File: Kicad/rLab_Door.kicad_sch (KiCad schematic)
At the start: 15 parts, among them J1 ACT_1, J10 I2C DISPLAY, J2 V_IN, J3 ACT_2, J4 BATTERY, J5 NPX_1, J6 NPX_2, J7 TAMPER, J8 WIEGAND KEYPAD, J9 NFC SERIAL

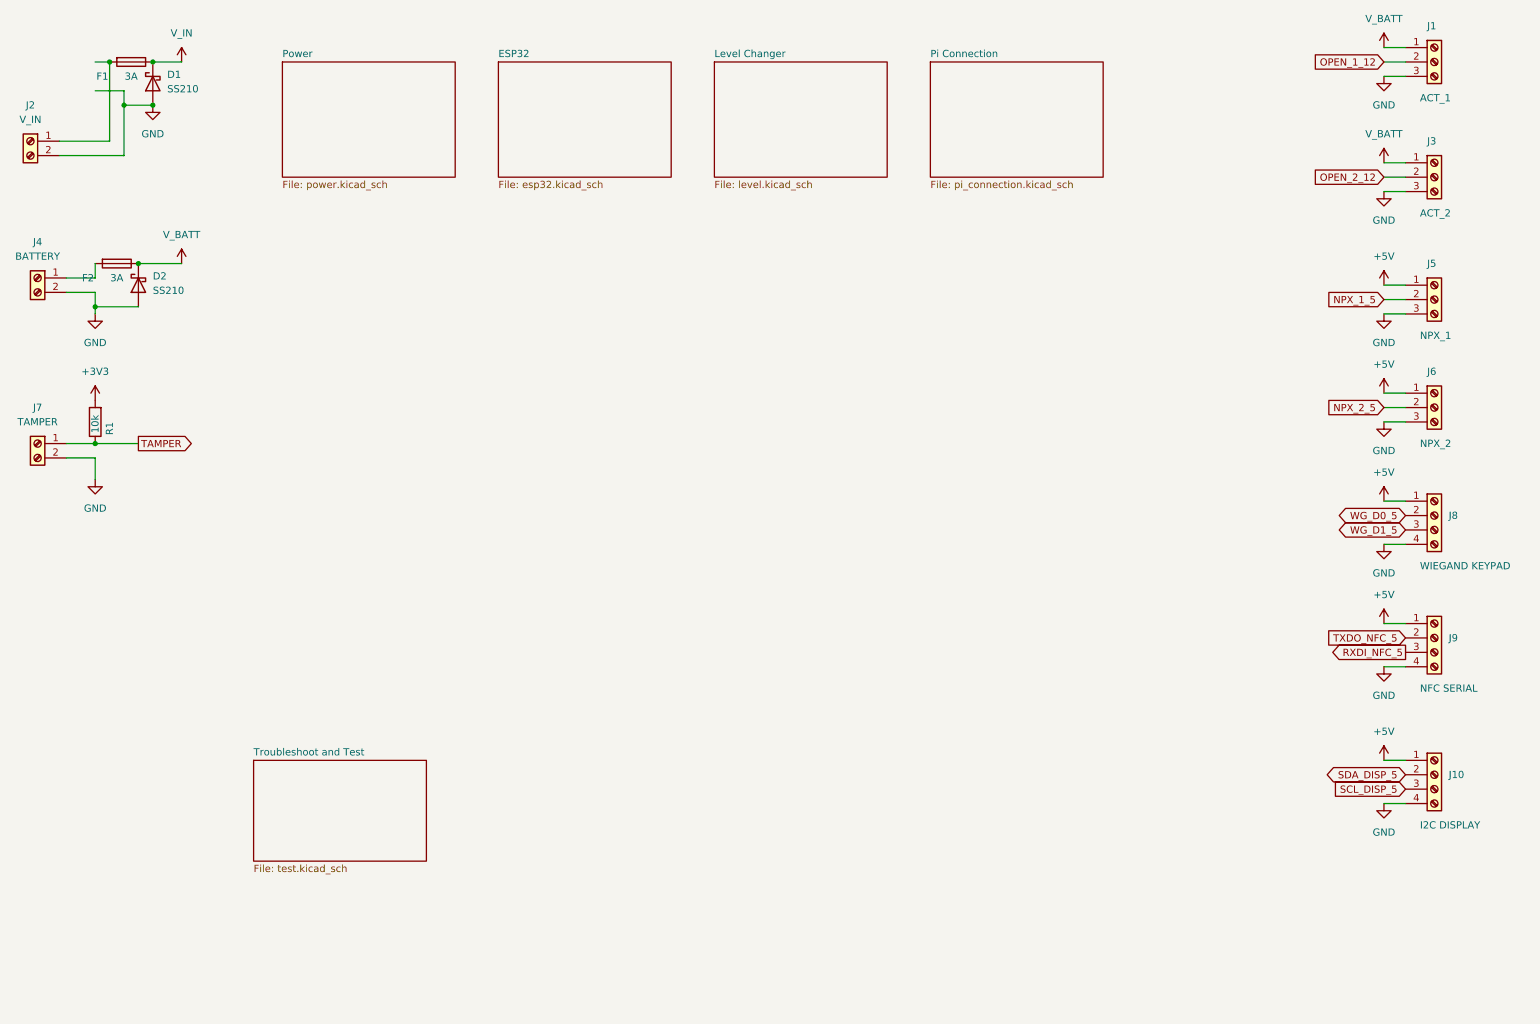
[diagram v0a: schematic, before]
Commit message: Rework of power circuits to improve protection
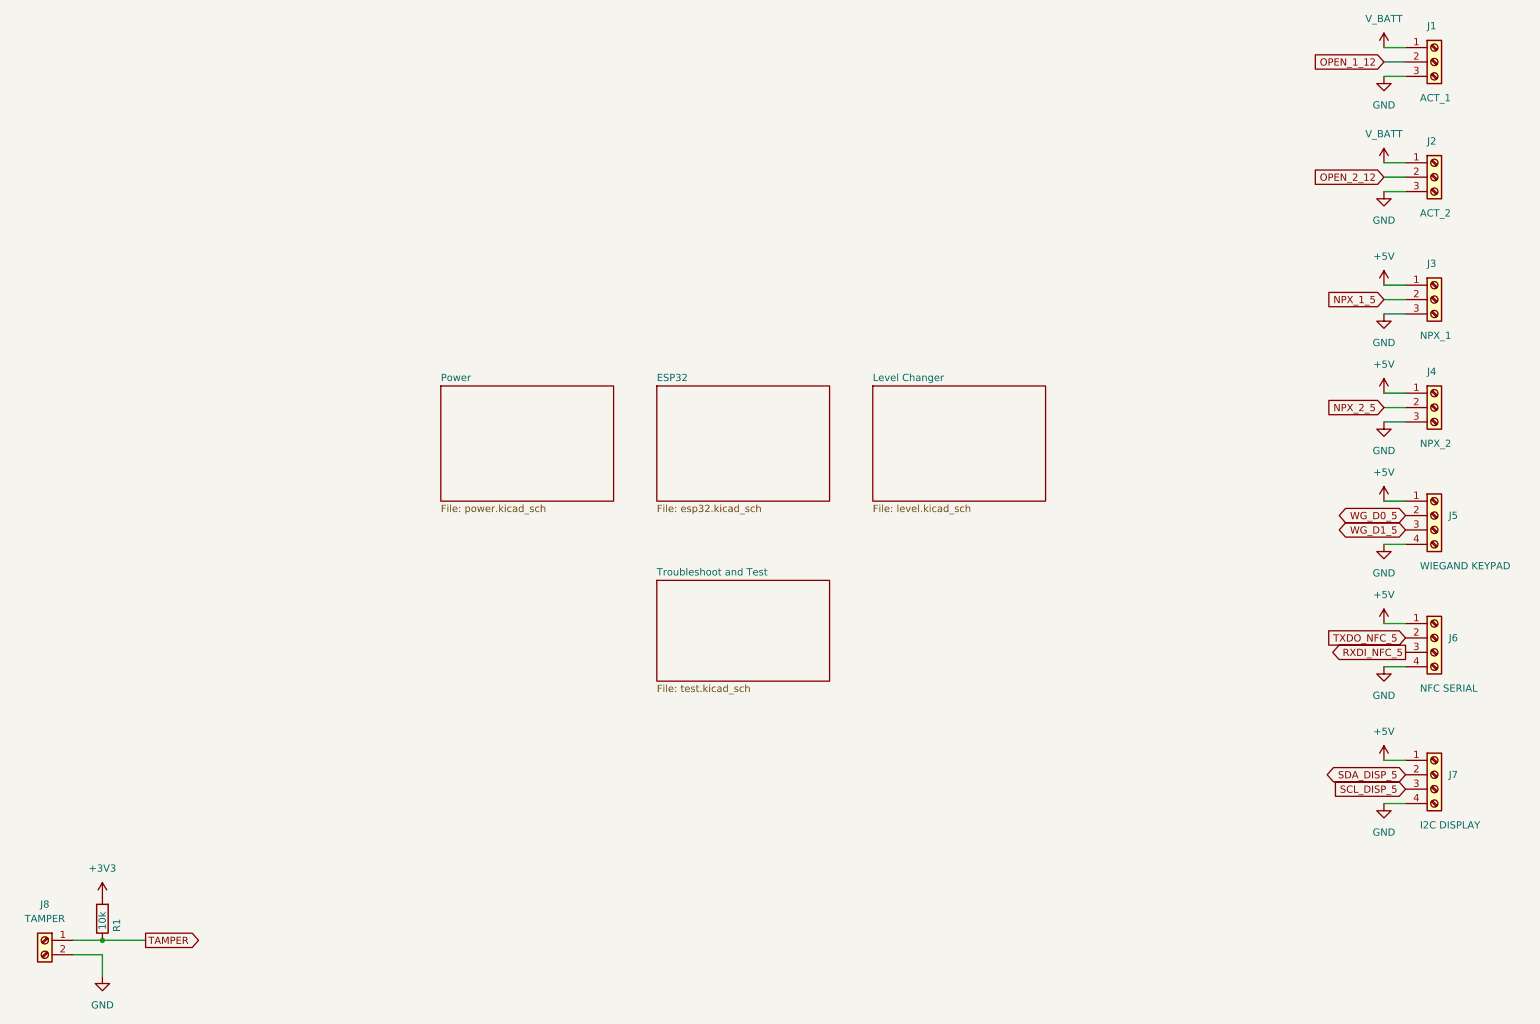
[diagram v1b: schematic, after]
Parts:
- removed D1, D2: SS210, Diode_SMD:D_SMA, symbol Device:D_Schottky
- removed F1, F2: 3A, Fuse:Fuseholder_Cylinder-5x20mm_Schurter_0031_8201_Horizontal_Open, symbol Device:Fuse
- removed J2: V_IN, TerminalBlock_Phoenix:TerminalBlock_Phoenix_MPT-0,5-2-2.54_1x02_P2.54mm_Horizontal, symbol Connector:Screw_Terminal_01x02
- removed J4: BATTERY, TerminalBlock_Phoenix:TerminalBlock_Phoenix_MPT-0,5-2-2.54_1x02_P2.54mm_Horizontal, symbol Connector:Screw_Terminal_01x02
- renumbered J3 to J2, J5 to J3, J6 to J4, J8 to J5, J9 to J6, J10 to J7, J7 to J8
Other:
- removed sheet Pi Connection
- moved on the sheet: J8, R1
